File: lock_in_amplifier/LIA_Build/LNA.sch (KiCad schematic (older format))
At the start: 47 parts, among them J17 RF_Shield_One_Piece, J38 RF_Shield_One_Piece, U6 lmp7721, U7 LM833, U8 AD8429

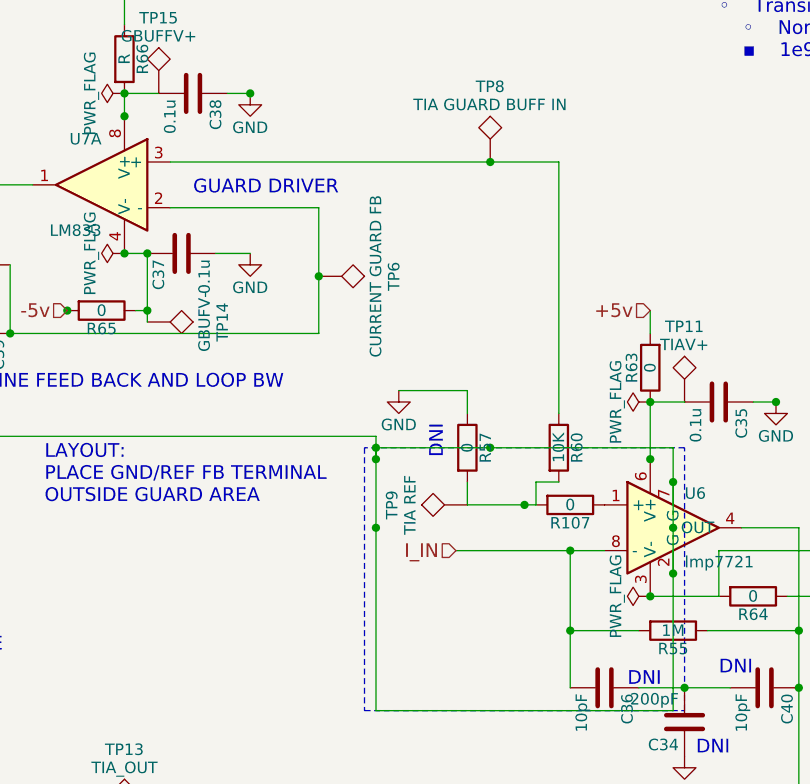
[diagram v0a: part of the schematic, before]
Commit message: initial lna and power floorplan finished.
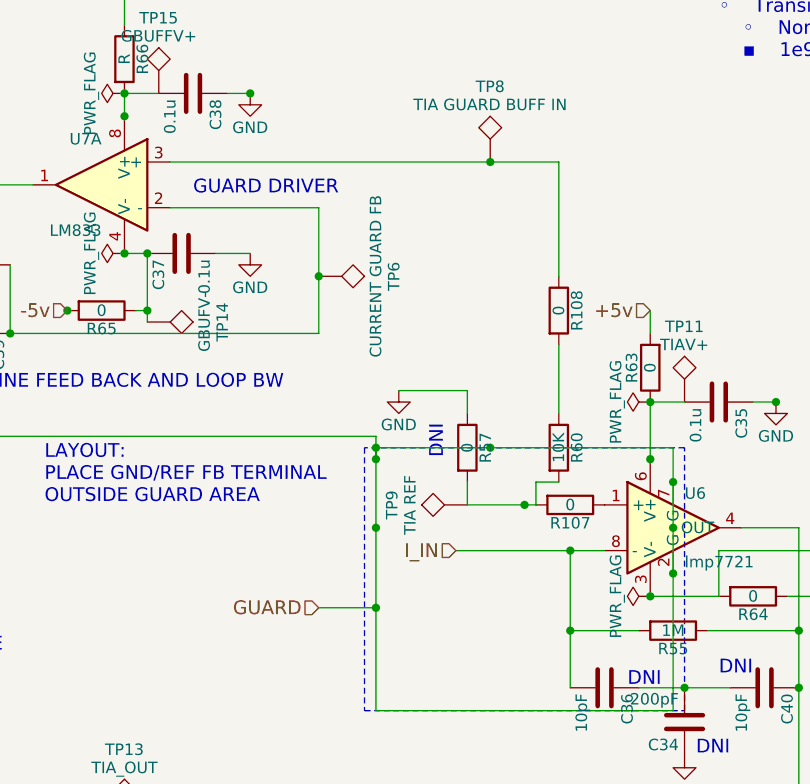
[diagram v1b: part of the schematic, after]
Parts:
- added R108: 0, Resistors_SMD:R_0805, symbol R
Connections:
- net GUARD: now reaches J17.1 (Shield), R56.1, R58.2, TP5.1, U6.2 (G), U6.7 (G)
- net at TP8.1, U7.3 (+): now also R108.1; no longer R60.1
- new net: R108.2, R60.1
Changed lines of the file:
@@
 LIBS:contrib
 LIBS:valves
+LIBS:ada2200
 LIBS:LIA-cache
-LIBS:LNA_test-cache
 EELAYER 25 0
 EELAYER END
 $Descr USLetter 11000 8500
 encoding utf-8
-Sheet 3 3
+Sheet 5 6
 Title "LNA AND TRANSIMPEDANCE AMPLIFIER"
 Date ""
@@
 $EndComp
 $Comp
-L GND #PWR042
+L GND #PWR073
 U 1 1 5A1C75B0
 P 4100 7200
-F 0 "#PWR042" H 4100 6950 50  0001 C CNN
+F 0 "#PWR073" H 4100 6950 50  0001 C CNN
 F 1 "GND" H 4100 7050 50  0000 C CNN
 F 2 "" H 4100 7200 50  0001 C CNN
@@
 $EndComp
 $Comp
-L GND #PWR043
+L GND #PWR074
 U 1 1 5A1C75B6
 P 5100 5900
-F 0 "#PWR043" H 5100 5650 50  0001 C CNN
+F 0 "#PWR074" H 5100 5650 50  0001 C CNN
 F 1 "GND" H 5100 5750 50  0000 C CNN
 F 2 "" H 5100 5900 50  0001 C CNN
@@
 TRANSIMPEDANCE AMPLIFIER
 $Comp
-L GND #PWR044
+L GND #PWR075
 U 1 1 5A1F5BDB
 P 1450 6950
-F 0 "#PWR044" H 1450 6700 50  0001 C CNN
+F 0 "#PWR075" H 1450 6700 50  0001 C CNN
 F 1 "GND" H 1450 6800 50  0000 C CNN
 F 2 "" H 1450 6950 50  0001 C CNN
@@
 $EndComp
 $Comp
-L GND #PWR045
+L GND #PWR076
 U 1 1 5A276A01
 P 5750 6900
-F 0 "#PWR045" H 5750 6650 50  0001 C CNN
+F 0 "#PWR076" H 5750 6650 50  0001 C CNN
 F 1 "GND" H 5750 6750 50  0000 C CNN
 F 2 "" H 5750 6900 50  0001 C CNN
@@
 $EndComp
 $Comp
-L GND #PWR046
+L GND #PWR077
 U 1 1 5A277FAE
 P 1100 6050
-F 0 "#PWR046" H 1100 5800 50  0001 C CNN
+F 0 "#PWR077" H 1100 5800 50  0001 C CNN
 F 1 "GND" H 1100 5900 50  0000 C CNN
 F 2 "" H 1100 6050 50  0001 C CNN
@@
 $EndComp
 $Comp
-L GND #PWR047
+L GND #PWR078
 U 1 1 5A277FE0
 P 1200 7050
-F 0 "#PWR047" H 1200 6800 50  0001 C CNN
+F 0 "#PWR078" H 1200 6800 50  0001 C CNN
 F 1 "GND" H 1200 6900 50  0000 C CNN
 F 2 "" H 1200 7050 50  0001 C CNN
@@
 $EndComp
 $Comp
-L GND #PWR048
+L GND #PWR079
 U 1 1 5A21D13B
 P 6850 3300
-F 0 "#PWR048" H 6850 3050 50  0001 C CNN
+F 0 "#PWR079" H 6850 3050 50  0001 C CNN
 F 1 "GND" H 6850 3150 50  0000 C CNN
 F 2 "" H 6850 3300 50  0001 C CNN
@@
 $EndComp
 $Comp
-L GND #PWR049
+L GND #PWR080
 U 1 1 5A21D39E
 P 6500 2450
-F 0 "#PWR049" H 6500 2200 50  0001 C CNN
+F 0 "#PWR080" H 6500 2200 50  0001 C CNN
 F 1 "GND" H 6500 2300 50  0000 C CNN
 F 2 "" H 6500 2450 50  0001 C CNN
@@
 GUARD DRIVER
 $Comp
-L GND #PWR050
+L GND #PWR081
 U 1 1 5A220C69
 P 4200 1100
-F 0 "#PWR050" H 4200 850 50  0001 C CNN
+F 0 "#PWR081" H 4200 850 50  0001 C CNN
 F 1 "GND" H 4200 950 50  0000 C CNN
 F 2 "" H 4200 1100 50  0001 C CNN
@@
 +5v
 $Comp
-L GND #PWR051
+L GND #PWR082
 U 1 1 5A220E76
 P 4200 1800
-F 0 "#PWR051" H 4200 1550 50  0001 C CNN
+F 0 "#PWR082" H 4200 1550 50  0001 C CNN
 F 1 "GND" H 4200 1650 50  0000 C CNN
 F 2 "" H 4200 1800 50  0001 C CNN
@@
 $EndComp
 $Comp
-L GND #PWR052
+L GND #PWR083
 U 1 1 5A221F33
 P 1550 2900
-F 0 "#PWR052" H 1550 2650 50  0001 C CNN
+F 0 "#PWR083" H 1550 2650 50  0001 C CNN
 F 1 "GND" H 1550 2750 50  0000 C CNN
 F 2 "" H 1550 2900 50  0001 C CNN
@@
 DNI
 $Comp
-L GND #PWR053
+L GND #PWR084
 U 1 1 5A2235D5
 P 4850 2400
-F 0 "#PWR053" H 4850 2150 50  0001 C CNN
+F 0 "#PWR084" H 4850 2150 50  0001 C CNN
 F 1 "GND" H 4850 2250 50  0000 C CNN
 F 2 "" H 4850 2400 50  0001 C CNN
@@
 DNI
 $Comp
-L GND #PWR054
+L GND #PWR085
 U 1 1 5A2424BB
 P 6100 4000
-F 0 "#PWR054" H 6100 3750 50  0001 C CNN
+F 0 "#PWR085" H 6100 3750 50  0001 C CNN
 F 1 "GND" H 6100 3850 50  0000 C CNN
 F 2 "" H 6100 4000 50  0001 C CNN
@@
 Wire Wire Line
 	5150 2400 5150 2500
-Wire Wire Line
-	5550 1400 5550 2500
 Wire Wire Line
 	3850 1400 5550 1400
@@
 Connection ~ 3400 2050
 $Comp
-L PWR_FLAG #FLG055
+L PWR_FLAG #FLG086
 U 1 1 5A2D348D
 P 3650 1100
-F 0 "#FLG055" H 3650 1175 50  0001 C CNN
+F 0 "#FLG086" H 3650 1175 50  0001 C CNN
 F 1 "PWR_FLAG" H 3650 1250 50  0000 C CNN
 F 2 "" H 3650 1100 50  0001 C CNN
@@
 $EndComp
 $Comp
-L PWR_FLAG #FLG056
+L PWR_FLAG #FLG087
 U 1 1 5A2D35B5
 P 3650 1800
-F 0 "#FLG056" H 3650 1875 50  0001 C CNN
+F 0 "#FLG087" H 3650 1875 50  0001 C CNN
 F 1 "PWR_FLAG" H 3650 1950 50  0000 C CNN
 F 2 "" H 3650 1800 50  0001 C CNN
@@
 $EndComp
 $Comp
-L PWR_FLAG #FLG057
+L PWR_FLAG #FLG088
 U 1 1 5A2D36AF
 P 5950 2450
-F 0 "#FLG057" H 5950 2525 50  0001 C CNN
+F 0 "#FLG088" H 5950 2525 50  0001 C CNN
 F 1 "PWR_FLAG" H 5950 2600 50  0000 C CNN
 F 2 "" H 5950 2450 50  0001 C CNN
@@
 $EndComp
 $Comp
-L PWR_FLAG #FLG058
+L PWR_FLAG #FLG089
 U 1 1 5A2D374D
 P 5950 3300
-F 0 "#FLG058" H 5950 3375 50  0001 C CNN
+F 0 "#FLG089" H 5950 3375 50  0001 C CNN
 F 1 "PWR_FLAG" H 5950 3450 50  0000 C CNN
 F 2 "" H 5950 3300 50  0001 C CNN
@@
 Wire Wire Line
 	1500 5950 1100 5950
+Text HLabel 4500 3350 0    60   Input ~ 0
+GUARD
+Wire Wire Line
+	4500 3350 4750 3350
+Connection ~ 4750 3350
+$Comp
+L R R108
+U 1 1 5A3480A8
+P 5550 2050
+F 0 "R108" V 5630 2050 50  0000 C CNN
+F 1 "0" V 5550 2050 50  0000 C CNN
+F 2 "Resistors_SMD:R_0805" V 5480 2050 50  0001 C CNN
+F 3 "" H 5550 2050 50  0001 C CNN
+	1    5550 2050
+	1    0    0    -1
+$EndComp
+Wire Wire Line
+	5550 2200 5550 2500
+Wire Wire Line
+	5550 1400 5550 1900
 $EndSCHEMATC

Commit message: initial LNA test layout
everything connected - moving towards a manufacturability test.
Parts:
- removed R64: 0, Resistors_SMD:R_0805, symbol R
- removed TP16: TIAV-, footprints:tyco_RCU_0603_Probe_Pad, symbol TEST
- removed TP9: TIA REF, footprints:tyco_RCU_0603_Probe_Pad, symbol TEST
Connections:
- net GND: now also U6.3 (V-)
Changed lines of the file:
@@
 LIBS:contrib
 LIBS:valves
-LIBS:ada2200
 LIBS:LIA-cache
+LIBS:LNA_test-cache
 EELAYER 25 0
 EELAYER END
 $Descr USLetter 11000 8500
 encoding utf-8
-Sheet 5 6
+Sheet 3 3
 Title "LNA AND TRANSIMPEDANCE AMPLIFIER"
 Date ""
@@
 $EndComp
 $Comp
-L GND #PWR073
+L GND #PWR041
 U 1 1 5A1C75B0
 P 4100 7200
-F 0 "#PWR073" H 4100 6950 50  0001 C CNN
+F 0 "#PWR041" H 4100 6950 50  0001 C CNN
 F 1 "GND" H 4100 7050 50  0000 C CNN
 F 2 "" H 4100 7200 50  0001 C CNN
@@
 $EndComp
 $Comp
-L GND #PWR074
+L GND #PWR042
 U 1 1 5A1C75B6
 P 5100 5900
-F 0 "#PWR074" H 5100 5650 50  0001 C CNN
+F 0 "#PWR042" H 5100 5650 50  0001 C CNN
 F 1 "GND" H 5100 5750 50  0000 C CNN
 F 2 "" H 5100 5900 50  0001 C CNN
@@
 TRANSIMPEDANCE AMPLIFIER
 $Comp
-L GND #PWR075
+L GND #PWR043
 U 1 1 5A1F5BDB
 P 1450 6950
-F 0 "#PWR075" H 1450 6700 50  0001 C CNN
+F 0 "#PWR043" H 1450 6700 50  0001 C CNN
 F 1 "GND" H 1450 6800 50  0000 C CNN
 F 2 "" H 1450 6950 50  0001 C CNN
@@
 $EndComp
 $Comp
-L GND #PWR076
+L GND #PWR044
 U 1 1 5A276A01
 P 5750 6900
-F 0 "#PWR076" H 5750 6650 50  0001 C CNN
+F 0 "#PWR044" H 5750 6650 50  0001 C CNN
 F 1 "GND" H 5750 6750 50  0000 C CNN
 F 2 "" H 5750 6900 50  0001 C CNN
@@
 $EndComp
 $Comp
-L GND #PWR077
+L GND #PWR045
 U 1 1 5A277FAE
 P 1100 6050
-F 0 "#PWR077" H 1100 5800 50  0001 C CNN
+F 0 "#PWR045" H 1100 5800 50  0001 C CNN
 F 1 "GND" H 1100 5900 50  0000 C CNN
 F 2 "" H 1100 6050 50  0001 C CNN
@@
 $EndComp
 $Comp
-L GND #PWR078
+L GND #PWR046
 U 1 1 5A277FE0
 P 1200 7050
-F 0 "#PWR078" H 1200 6800 50  0001 C CNN
+F 0 "#PWR046" H 1200 6800 50  0001 C CNN
 F 1 "GND" H 1200 6900 50  0000 C CNN
 F 2 "" H 1200 7050 50  0001 C CNN
@@
 $EndComp
 $Comp
-L GND #PWR079
+L GND #PWR047
 U 1 1 5A21D13B
 P 6850 3300
-F 0 "#PWR079" H 6850 3050 50  0001 C CNN
+F 0 "#PWR047" H 6850 3050 50  0001 C CNN
 F 1 "GND" H 6850 3150 50  0000 C CNN
 F 2 "" H 6850 3300 50  0001 C CNN
@@
 $EndComp
 $Comp
-L GND #PWR080
+L GND #PWR048
 U 1 1 5A21D39E
 P 6500 2450
-F 0 "#PWR080" H 6500 2200 50  0001 C CNN
+F 0 "#PWR048" H 6500 2200 50  0001 C CNN
 F 1 "GND" H 6500 2300 50  0000 C CNN
 F 2 "" H 6500 2450 50  0001 C CNN
@@
 GUARD DRIVER
 $Comp
-L GND #PWR081
+L GND #PWR049
 U 1 1 5A220C69
 P 4200 1100
-F 0 "#PWR081" H 4200 850 50  0001 C CNN
+F 0 "#PWR049" H 4200 850 50  0001 C CNN
 F 1 "GND" H 4200 950 50  0000 C CNN
 F 2 "" H 4200 1100 50  0001 C CNN
@@
 +5v
 $Comp
-L GND #PWR082
+L GND #PWR050
 U 1 1 5A220E76
 P 4200 1800
-F 0 "#PWR082" H 4200 1550 50  0001 C CNN
+F 0 "#PWR050" H 4200 1550 50  0001 C CNN
 F 1 "GND" H 4200 1650 50  0000 C CNN
 F 2 "" H 4200 1800 50  0001 C CNN
@@
 $EndComp
 $Comp
-L GND #PWR083
+L GND #PWR051
 U 1 1 5A221F33
 P 1550 2900
-F 0 "#PWR083" H 1550 2650 50  0001 C CNN
+F 0 "#PWR051" H 1550 2650 50  0001 C CNN
 F 1 "GND" H 1550 2750 50  0000 C CNN
 F 2 "" H 1550 2900 50  0001 C CNN
@@
 DNI
 $Comp
-L GND #PWR084
+L GND #PWR052
 U 1 1 5A2235D5
 P 4850 2400
-F 0 "#PWR084" H 4850 2150 50  0001 C CNN
+F 0 "#PWR052" H 4850 2150 50  0001 C CNN
 F 1 "GND" H 4850 2250 50  0000 C CNN
 F 2 "" H 4850 2400 50  0001 C CNN
@@
 	1    4500 1900
 	0    1    1    0
-$EndComp
-$Comp
-L TEST TP9
-U 1 1 5A23ED84
-P 5150 2900
-F 0 "TP9" H 5150 3200 50  0000 C BNN
-F 1 "TIA REF" H 5150 3150 50  0000 C CNN
-F 2 "footprints:tyco_RCU_0603_Probe_Pad" H 5150 2900 50  0001 C CNN
-F 3 "" H 5150 2900 50  0001 C CNN
-	1    5150 2900
-	0    -1   -1   0
 $EndComp
 $Comp
@@
 DNI
 $Comp
-L GND #PWR085
+L GND #PWR053
 U 1 1 5A2424BB
 P 6100 4000
-F 0 "#PWR085" H 6100 3750 50  0001 C CNN
+F 0 "#PWR053" H 6100 3750 50  0001 C CNN
 F 1 "GND" H 6100 3850 50  0000 C CNN
 F 2 "" H 6100 4000 50  0001 C CNN
@@
 	1    6100 4000
 	-1   0    0    -1
-$EndComp
-$Comp
-L R R64
-U 1 1 5A242E8C
-P 6400 3300
-F 0 "R64" V 6480 3300 50  0000 C CNN
-F 1 "0" V 6400 3300 50  0000 C CNN
-F 2 "Resistors_SMD:R_0805" V 6330 3300 50  0001 C CNN
-F 3 "" H 6400 3300 50  0001 C CNN
-	1    6400 3300
-	0    1    1    0
 $EndComp
 $Comp
@@
 Connection ~ 6100 3700
 Wire Wire Line
-	5950 3300 6250 3300
-Wire Wire Line
-	6550 3300 6850 3300
+	5950 3300 6850 3300
 Wire Wire Line
 	5950 2050 5950 2150
@@
 	1    0    0    -1
 $EndComp
-$Comp
-L TEST TP16
-U 1 1 5A245507
-P 6750 3100
-F 0 "TP16" H 6750 3400 50  0000 C BNN
-F 1 "TIAV-" H 6750 3350 50  0000 C CNN
-F 2 "footprints:tyco_RCU_0603_Probe_Pad" H 6750 3100 50  0001 C CNN
-F 3 "" H 6750 3100 50  0001 C CNN
-	1    6750 3100
-	0    1    1    0
-$EndComp
-Wire Wire Line
-	6750 3100 6250 3100
-Wire Wire Line
-	6250 3100 6250 3300
 $Comp
 L TEST TP13
@@
 Connection ~ 3400 2050
 $Comp
-L PWR_FLAG #FLG086
+L PWR_FLAG #FLG054
 U 1 1 5A2D348D
 P 3650 1100
-F 0 "#FLG086" H 3650 1175 50  0001 C CNN
+F 0 "#FLG054" H 3650 1175 50  0001 C CNN
 F 1 "PWR_FLAG" H 3650 1250 50  0000 C CNN
 F 2 "" H 3650 1100 50  0001 C CNN
@@
 $EndComp
 $Comp
-L PWR_FLAG #FLG087
+L PWR_FLAG #FLG055
 U 1 1 5A2D35B5
 P 3650 1800
-F 0 "#FLG087" H 3650 1875 50  0001 C CNN
+F 0 "#FLG055" H 3650 1875 50  0001 C CNN
 F 1 "PWR_FLAG" H 3650 1950 50  0000 C CNN
 F 2 "" H 3650 1800 50  0001 C CNN
@@
 $EndComp
 $Comp
-L PWR_FLAG #FLG088
+L PWR_FLAG #FLG056
 U 1 1 5A2D36AF
 P 5950 2450
-F 0 "#FLG088" H 5950 2525 50  0001 C CNN
+F 0 "#FLG056" H 5950 2525 50  0001 C CNN
 F 1 "PWR_FLAG" H 5950 2600 50  0000 C CNN
 F 2 "" H 5950 2450 50  0001 C CNN
@@
 $EndComp
 $Comp
-L PWR_FLAG #FLG089
+L PWR_FLAG #FLG057
 U 1 1 5A2D374D
 P 5950 3300
-F 0 "#FLG089" H 5950 3375 50  0001 C CNN
+F 0 "#FLG057" H 5950 3375 50  0001 C CNN
 F 1 "PWR_FLAG" H 5950 3450 50  0000 C CNN
 F 2 "" H 5950 3300 50  0001 C CNN

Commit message: correct lmp7721 package - soic
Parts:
- U6: footprint Housings_SSOP:MSOP-8-1EP_3x3mm_Pitch0.65mm -> Housings_SOIC:SOIC-8_3.9x4.9mm_Pitch1.27mm
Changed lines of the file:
@@
 F 0 "U6" H 6100 3150 50  0000 L CNN
 F 1 "lmp7721" H 6100 2850 50  0000 L CNN
-F 2 "Housings_SSOP:MSOP-8-1EP_3x3mm_Pitch0.65mm" H 6300 2700 50  0001 C CNN
+F 2 "Housings_SOIC:SOIC-8_3.9x4.9mm_Pitch1.27mm" H 6300 2700 50  0001 C CNN
 F 3 "" H 6050 3200 50  0001 C CNN
 	1    6050 3000

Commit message: adressing comments - fets
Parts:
- removed C34: 200pF, Capacitors_SMD:C_0805, symbol C
- removed C40: 10pF, Capacitors_SMD:C_0805, symbol C
- removed R107: 0, Resistors_SMD:R_0805, symbol R
- added R64: 100, Resistors_SMD:R_0805, symbol R
- R55: value 1M -> 100M
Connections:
- net I_IN: now also R64.2; no longer C36.2, R55.2, U6.8 (-)
- net at R55.1, S4.1 (B1), TP13.1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: now also C36.1
- net at R57.2, R60.2: now also U6.1 (+)
- new net: C36.2, R55.2, R64.1, U6.8 (-)
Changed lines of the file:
@@
 LIBS:contrib
 LIBS:valves
+LIBS:ada2200
 LIBS:LIA-cache
-LIBS:LNA_test-cache
 EELAYER 25 0
 EELAYER END
 $Descr USLetter 11000 8500
 encoding utf-8
-Sheet 3 3
+Sheet 3 6
 Title "LNA AND TRANSIMPEDANCE AMPLIFIER"
 Date ""
@@
 $EndComp
 $Comp
-L GND #PWR041
+L GND #PWR73
 U 1 1 5A1C75B0
 P 4100 7200
-F 0 "#PWR041" H 4100 6950 50  0001 C CNN
+F 0 "#PWR73" H 4100 6950 50  0001 C CNN
 F 1 "GND" H 4100 7050 50  0000 C CNN
 F 2 "" H 4100 7200 50  0001 C CNN
@@
 $EndComp
 $Comp
-L GND #PWR042
+L GND #PWR77
 U 1 1 5A1C75B6
 P 5100 5900
-F 0 "#PWR042" H 5100 5650 50  0001 C CNN
+F 0 "#PWR77" H 5100 5650 50  0001 C CNN
 F 1 "GND" H 5100 5750 50  0000 C CNN
 F 2 "" H 5100 5900 50  0001 C CNN
@@
 TRANSIMPEDANCE AMPLIFIER
 $Comp
-L GND #PWR043
+L GND #PWR71
 U 1 1 5A1F5BDB
 P 1450 6950
-F 0 "#PWR043" H 1450 6700 50  0001 C CNN
+F 0 "#PWR71" H 1450 6700 50  0001 C CNN
 F 1 "GND" H 1450 6800 50  0000 C CNN
 F 2 "" H 1450 6950 50  0001 C CNN
@@
 $EndComp
 $Comp
-L GND #PWR044
+L GND #PWR78
 U 1 1 5A276A01
 P 5750 6900
-F 0 "#PWR044" H 5750 6650 50  0001 C CNN
+F 0 "#PWR78" H 5750 6650 50  0001 C CNN
 F 1 "GND" H 5750 6750 50  0000 C CNN
 F 2 "" H 5750 6900 50  0001 C CNN
@@
 $EndComp
 $Comp
-L GND #PWR045
+L GND #PWR69
 U 1 1 5A277FAE
 P 1100 6050
-F 0 "#PWR045" H 1100 5800 50  0001 C CNN
+F 0 "#PWR69" H 1100 5800 50  0001 C CNN
 F 1 "GND" H 1100 5900 50  0000 C CNN
 F 2 "" H 1100 6050 50  0001 C CNN
@@
 $EndComp
 $Comp
-L GND #PWR046
+L GND #PWR70
 U 1 1 5A277FE0
 P 1200 7050
-F 0 "#PWR046" H 1200 6800 50  0001 C CNN
+F 0 "#PWR70" H 1200 6800 50  0001 C CNN
 F 1 "GND" H 1200 6900 50  0000 C CNN
 F 2 "" H 1200 7050 50  0001 C CNN
@@
 $EndComp
 $Comp
-L GND #PWR047
+L GND #PWR80
 U 1 1 5A21D13B
 P 6850 3300
-F 0 "#PWR047" H 6850 3050 50  0001 C CNN
+F 0 "#PWR80" H 6850 3050 50  0001 C CNN
 F 1 "GND" H 6850 3150 50  0000 C CNN
 F 2 "" H 6850 3300 50  0001 C CNN
@@
 $EndComp
 $Comp
-L GND #PWR048
+L GND #PWR79
 U 1 1 5A21D39E
 P 6500 2450
-F 0 "#PWR048" H 6500 2200 50  0001 C CNN
+F 0 "#PWR79" H 6500 2200 50  0001 C CNN
 F 1 "GND" H 6500 2300 50  0000 C CNN
 F 2 "" H 6500 2450 50  0001 C CNN
@@
 P 6050 3450
 F 0 "R55" V 6130 3450 50  0000 C CNN
-F 1 "1M" V 6050 3450 50  0000 C CNN
+F 1 "100M" V 6050 3450 50  0000 C CNN
 F 2 "Resistors_SMD:R_0805" V 5980 3450 50  0001 C CNN
 F 3 "" H 6050 3450 50  0001 C CNN
@@
 GUARD DRIVER
 $Comp
-L GND #PWR049
+L GND #PWR74
 U 1 1 5A220C69
 P 4200 1100
-F 0 "#PWR049" H 4200 850 50  0001 C CNN
+F 0 "#PWR74" H 4200 850 50  0001 C CNN
 F 1 "GND" H 4200 950 50  0000 C CNN
 F 2 "" H 4200 1100 50  0001 C CNN
@@
 +5v
 $Comp
-L GND #PWR050
+L GND #PWR75
 U 1 1 5A220E76
 P 4200 1800
-F 0 "#PWR050" H 4200 1550 50  0001 C CNN
+F 0 "#PWR75" H 4200 1550 50  0001 C CNN
 F 1 "GND" H 4200 1650 50  0000 C CNN
 F 2 "" H 4200 1800 50  0001 C CNN
@@
 $EndComp
 $Comp
-L GND #PWR051
+L GND #PWR72
 U 1 1 5A221F33
 P 1550 2900
-F 0 "#PWR051" H 1550 2650 50  0001 C CNN
+F 0 "#PWR72" H 1550 2650 50  0001 C CNN
 F 1 "GND" H 1550 2750 50  0000 C CNN
 F 2 "" H 1550 2900 50  0001 C CNN
@@
 DNI
 $Comp
-L GND #PWR052
+L GND #PWR76
 U 1 1 5A2235D5
 P 4850 2400
-F 0 "#PWR052" H 4850 2150 50  0001 C CNN
+F 0 "#PWR76" H 4850 2150 50  0001 C CNN
 F 1 "GND" H 4850 2250 50  0000 C CNN
 F 2 "" H 4850 2400 50  0001 C CNN
@@
 	1    0    0    -1
 $EndComp
-$Comp
-L C C40
-U 1 1 5A2420E6
-P 6450 3700
-F 0 "C40" H 6475 3800 50  0000 L CNN
-F 1 "10pF" H 6475 3600 50  0000 L CNN
-F 2 "Capacitors_SMD:C_0805" H 6488 3550 50  0001 C CNN
-F 3 "" H 6450 3700 50  0001 C CNN
-	1    6450 3700
-	0    1    1    0
-$EndComp
-$Comp
-L C C34
-U 1 1 5A2421FA
-P 6100 3850
-F 0 "C34" H 6125 3950 50  0000 L CNN
-F 1 "200pF" H 6125 3750 50  0000 L CNN
-F 2 "Capacitors_SMD:C_0805" H 6138 3700 50  0001 C CNN
-F 3 "" H 6100 3850 50  0001 C CNN
-	1    6100 3850
-	-1   0    0    1
-$EndComp
 Text Notes 6150 4000 0    60   ~ 0
 DNI
 Text Notes 6250 3650 0    60   ~ 0
 DNI
-$Comp
-L GND #PWR053
-U 1 1 5A2424BB
-P 6100 4000
-F 0 "#PWR053" H 6100 3750 50  0001 C CNN
-F 1 "GND" H 6100 3850 50  0000 C CNN
-F 2 "" H 6100 4000 50  0001 C CNN
-F 3 "" H 6100 4000 50  0001 C CNN
-	1    6100 4000
-	-1   0    0    -1
-$EndComp
 $Comp
 L R R63
@@
 Connection ~ 5250 2650
 Wire Wire Line
-	5100 3100 5750 3100
-Wire Wire Line
 	4750 2600 4750 3800
 Wire Wire Line
@@
 Connection ~ 6050 2800
 Wire Wire Line
-	5150 2900 5450 2900
+	5150 2900 5750 2900
 Connection ~ 4750 2650
 Connection ~ 1550 2600
@@
 Connection ~ 5250 1400
 Connection ~ 5400 2900
-Wire Wire Line
-	5900 3700 6300 3700
-Connection ~ 6100 3700
 Wire Wire Line
 	5950 3300 6850 3300
@@
 Connection ~ 3400 2050
 $Comp
-L PWR_FLAG #FLG054
+L PWR_FLAG #FLG9
 U 1 1 5A2D348D
 P 3650 1100
-F 0 "#FLG054" H 3650 1175 50  0001 C CNN
+F 0 "#FLG9" H 3650 1175 50  0001 C CNN
 F 1 "PWR_FLAG" H 3650 1250 50  0000 C CNN
 F 2 "" H 3650 1100 50  0001 C CNN
@@
 $EndComp
 $Comp
-L PWR_FLAG #FLG055
+L PWR_FLAG #FLG10
 U 1 1 5A2D35B5
 P 3650 1800
-F 0 "#FLG055" H 3650 1875 50  0001 C CNN
+F 0 "#FLG10" H 3650 1875 50  0001 C CNN
 F 1 "PWR_FLAG" H 3650 1950 50  0000 C CNN
 F 2 "" H 3650 1800 50  0001 C CNN
@@
 $EndComp
 $Comp
-L PWR_FLAG #FLG056
+L PWR_FLAG #FLG11
 U 1 1 5A2D36AF
 P 5950 2450
-F 0 "#FLG056" H 5950 2525 50  0001 C CNN
+F 0 "#FLG11" H 5950 2525 50  0001 C CNN
 F 1 "PWR_FLAG" H 5950 2600 50  0000 C CNN
 F 2 "" H 5950 2450 50  0001 C CNN
@@
 $EndComp
 $Comp
-L PWR_FLAG #FLG057
+L PWR_FLAG #FLG12
 U 1 1 5A2D374D
 P 5950 3300
-F 0 "#FLG057" H 5950 3375 50  0001 C CNN
+F 0 "#FLG12" H 5950 3375 50  0001 C CNN
 F 1 "PWR_FLAG" H 5950 3450 50  0000 C CNN
 F 2 "" H 5950 3300 50  0001 C CNN
@@
 	1    5950 3300
 	0    -1   -1   0
-$EndComp
-$Comp
-L R R107
-U 1 1 5A3351D4
-P 5600 2900
-F 0 "R107" V 5680 2900 50  0000 C CNN
-F 1 "0" V 5600 2900 50  0000 C CNN
-F 2 "Resistors_SMD:R_0805" V 5530 2900 50  0001 C CNN
-F 3 "" H 5600 2900 50  0001 C CNN
-	1    5600 2900
-	0    1    1    0
 $EndComp
 Wire Wire Line
@@
 Wire Wire Line
 	5550 1400 5550 1900
+$Comp
+L R R64
+U 1 1 5A3975B2
+P 5350 3100
+F 0 "R64" V 5430 3100 50  0000 C CNN
+F 1 "100" V 5350 3100 50  0000 C CNN
+F 2 "Resistors_SMD:R_0805" V 5280 3100 50  0001 C CNN
+F 3 "" H 5350 3100 50  0001 C CNN
+	1    5350 3100
+	0    1    1    0
+$EndComp
+Wire Wire Line
+	5100 3100 5200 3100
+Wire Wire Line
+	5500 3100 5750 3100
+Wire Wire Line
+	5900 3700 6600 3700
+Connection ~ 5450 2900
 $EndSCHEMATC
